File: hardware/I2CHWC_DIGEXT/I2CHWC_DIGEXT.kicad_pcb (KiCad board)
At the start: 2 copper layers, 66 x 99.1 mm, 67 parts, among them J1 Encoders 11-20, J2 Encoders 21-30, J3 EXT

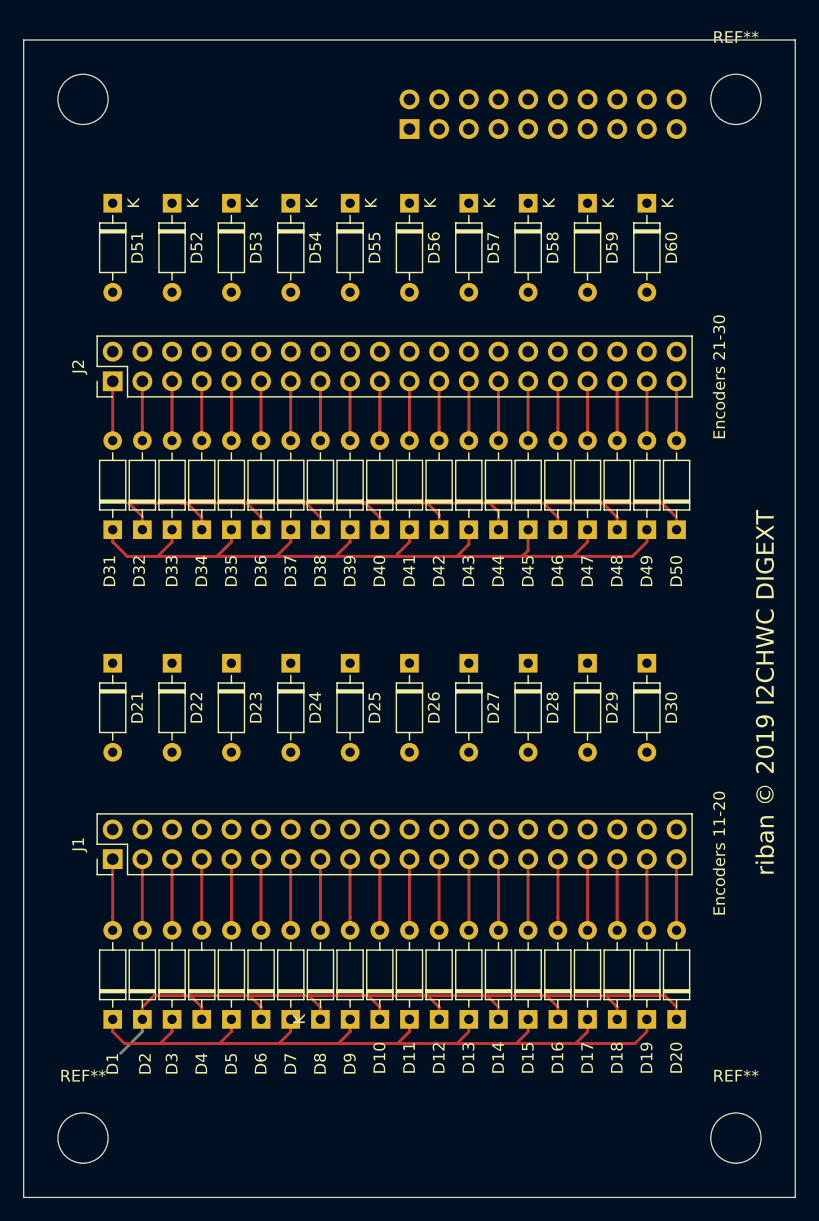
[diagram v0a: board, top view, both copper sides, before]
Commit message: Firmwware changes: Temporarily disable ADC (whilst investigating noise issues). Change quantity of switches (from 60 to 50). Start implementing I2C commands (wip). Reverse encoder rotation (maybe just the hardware implementation of the prototype - need to validate with schematics). Schematic and PCB improvements (wip): Separate out main and extender boards to separate projects / folders. Main board now supports 10 encoders with switches, 20 switches and 8 ADC plus detection of ADC multiplex and I2C address. Extension board for encoders 11 - 30. Extension board for ADC 1 - 64.
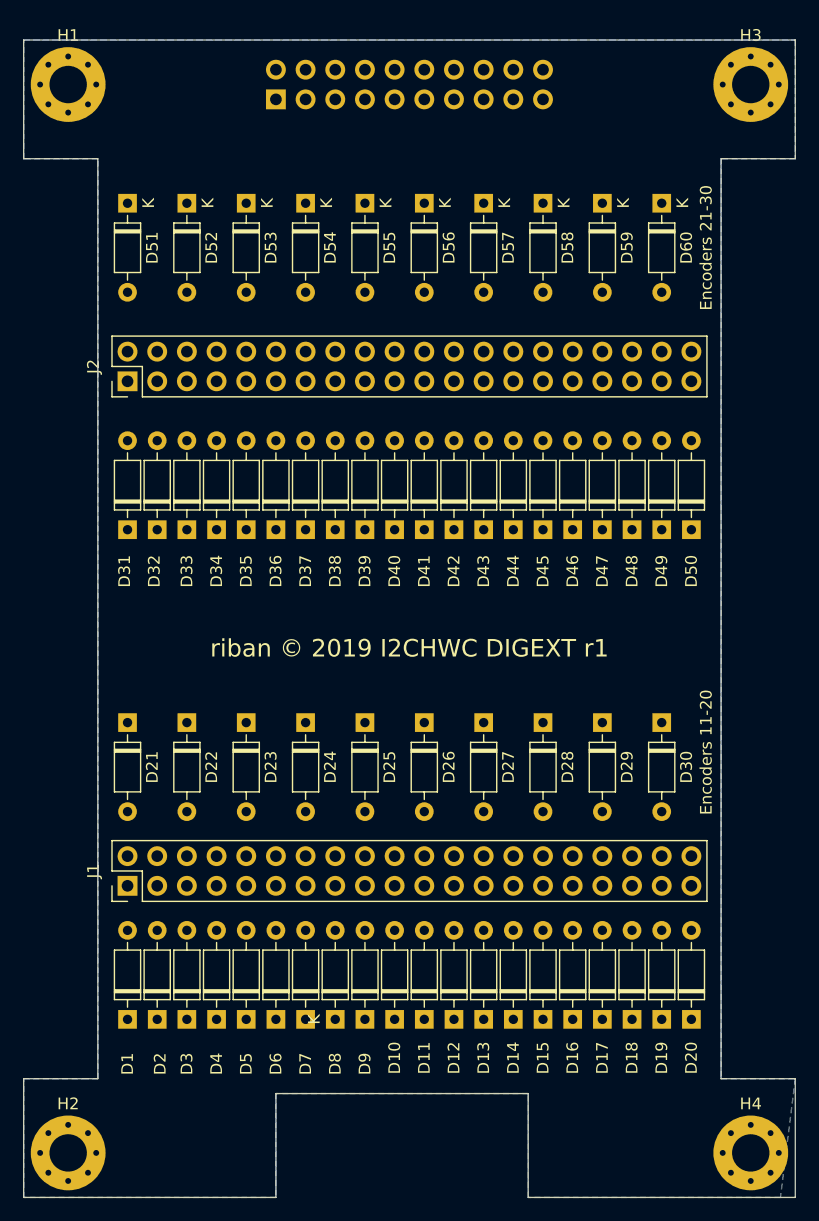
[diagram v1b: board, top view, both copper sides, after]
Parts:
- removed REF** (x4): MountingHole_4.3mm_M4, MountingHole:MountingHole_4.3mm_M4
- added H1: MountingHole_Pad, MountingHole:MountingHole_3.2mm_M3_Pad_Via, F.Cu at (52.1, 34.3)
- added H2: MountingHole_Pad, MountingHole:MountingHole_3.2mm_M3_Pad_Via, F.Cu at (52.1, 125.7)
- added H3: MountingHole_Pad, MountingHole:MountingHole_3.2mm_M3_Pad_Via, F.Cu at (110.5, 34.3)
- added H4: MountingHole_Pad, MountingHole:MountingHole_3.2mm_M3_Pad_Via, F.Cu at (110.5, 125.7)
- moved J3 11.7 mm to (69.8, 35.6)
- moved D29 5.24 mm to (97.8, 88.9)
- moved D30 5.24 mm to (102.9, 88.9)
- moved D21 5.24 mm to (57.1, 88.9)
- moved D22 5.24 mm to (62.2, 88.9)
- moved D23 5.24 mm to (67.3, 88.9)
- moved D24 5.24 mm to (72.4, 88.9)
- moved D25 5.24 mm to (77.5, 88.9)
- moved D26 5.24 mm to (82.5, 88.9)
- moved D27 5.24 mm to (87.6, 88.9)
- moved D28 5.24 mm to (92.7, 88.9)
- moved J1 2.62 mm to (57.1, 102.9)
- moved D10 1.27 mm to (80.0, 114.3)
- moved D12 1.27 mm to (85.1, 114.3)
- moved D17 1.27 mm to (97.8, 114.3)
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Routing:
- net EncIn3a: track 75.5 -> 0.00 mm
- net EncIn2a: track 74.7 -> 0.00 mm
- net SwitchIn2: track 72.1 -> 0.00 mm
- net SwitchIn3: track 71.4 -> 0.00 mm
- net Net-(D9-Pad2): track 6.10 -> 0.00 mm
- net Net-(D8-Pad2): track 6.10 -> 0.00 mm
- net Net-(D7-Pad2): track 6.10 -> 0.00 mm
- net Net-(D6-Pad2): track 6.10 -> 0.00 mm
- net Net-(D5-Pad2): track 6.10 -> 0.00 mm
- net Net-(D4-Pad2): track 6.10 -> 0.00 mm
- net Net-(D3-Pad2): track 6.10 -> 0.00 mm
- net Net-(D20-Pad2): track 6.10 -> 0.00 mm
- net Net-(D2-Pad2): track 6.10 -> 0.00 mm
- net Net-(D19-Pad2): track 6.10 -> 0.00 mm
- net Net-(D18-Pad2): track 6.10 -> 0.00 mm
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- added copper zone on B.Cu, net GND
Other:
- outline, holes or cut-outs redrawn
- board text added: "riban © 2019 I2CHWC DIGEXT r1"
- board text removed: "riban © 2019 I2CHWC DIGEXT"
